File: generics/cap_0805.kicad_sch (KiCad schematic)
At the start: 2 parts

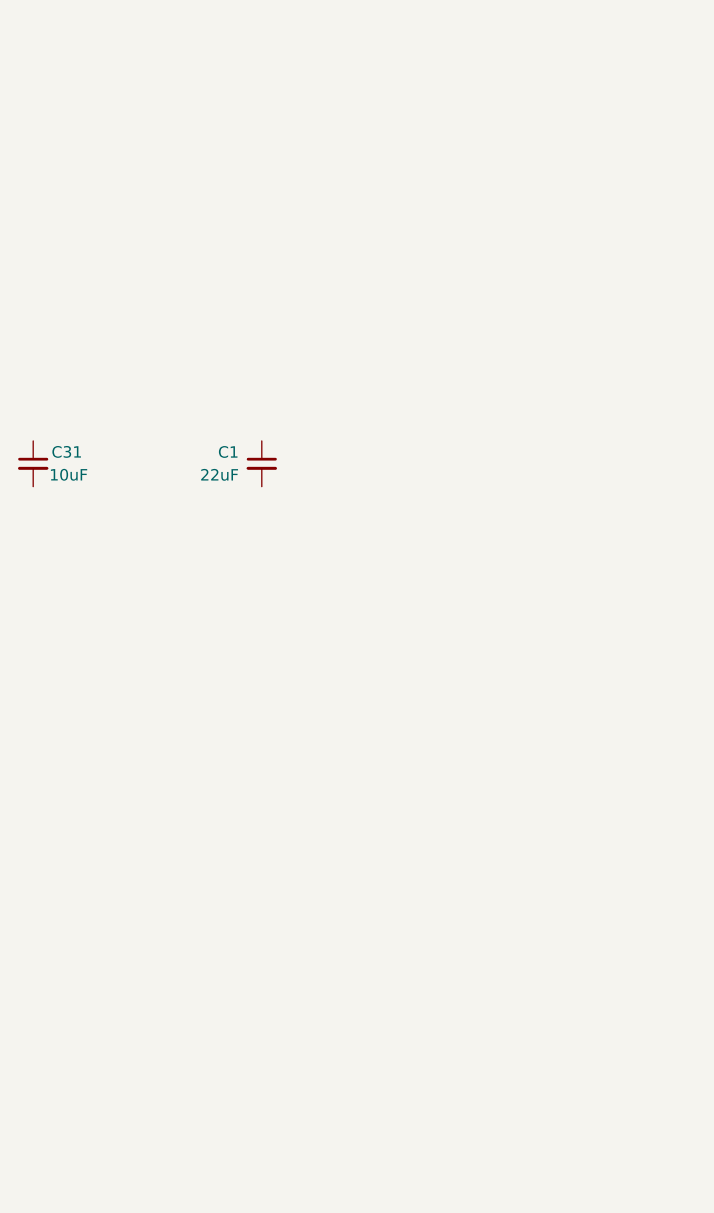
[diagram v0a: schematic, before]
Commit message: Add ESP32 and relevant peripherals
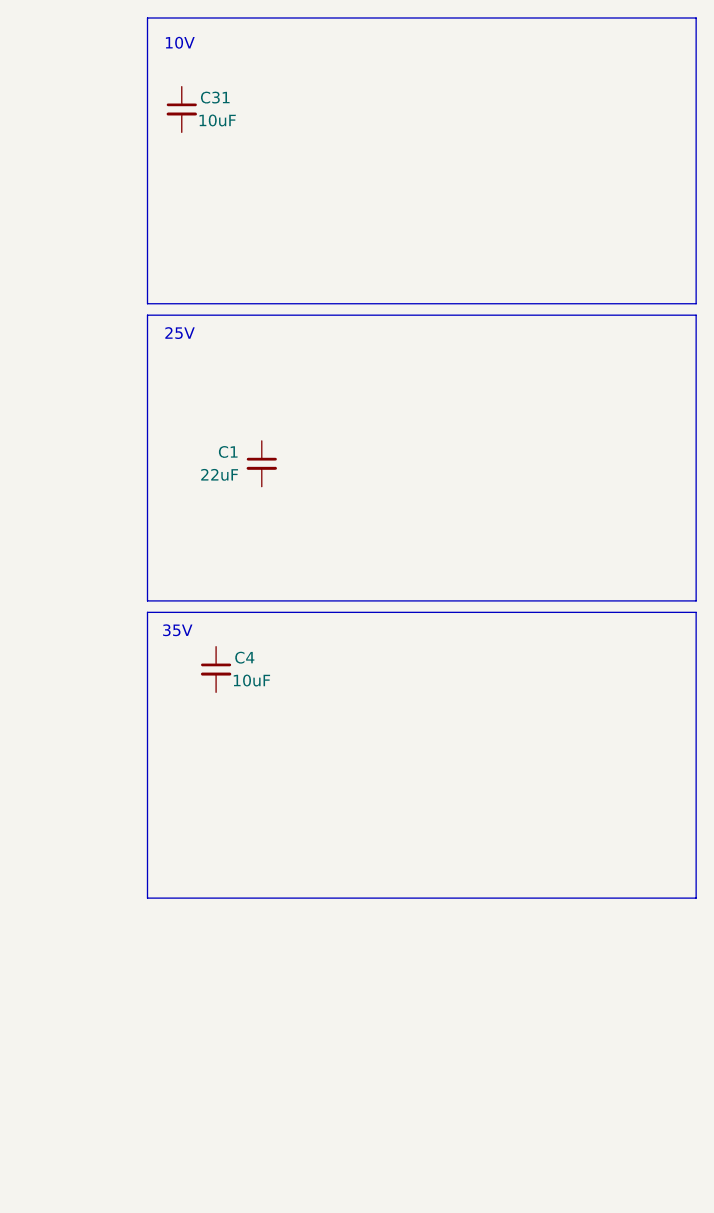
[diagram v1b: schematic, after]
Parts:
- added C4: 10uF, Capacitor_SMD:C_0805_2012Metric, symbol Device:C_Small
- C1: Tolerance (none) -> 20%; Votlage (none) -> 25V
- C31: Tolerance (none) -> 10%; Voltage (none) -> 10V
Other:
- note added: "10V"
- note added: "25V"
- note added: "35V"
- moved on the sheet: C31
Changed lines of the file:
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@@
 	(generator_version "9.0")
 	(paper "A4")
+	(rectangle
+		(start 31.75 20.32)
+		(end 92.71 52.07)
+		(stroke
+			(width 0)
+			(type default)
+		)
+		(fill
+			(type none)
+		)
+	)
+	(rectangle
+		(start 31.75 86.36)
+		(end 92.71 118.11)
+		(stroke
+			(width 0)
+			(type default)
+		)
+		(fill
+			(type none)
+		)
+	)
+	(rectangle
+		(start 31.75 53.34)
+		(end 92.71 85.09)
+		(stroke
+			(width 0)
+			(type default)
+		)
+		(fill
+			(type none)
+		)
+	)
+	(text "10V"
+		(exclude_from_sim no)
+		(at 35.306 23.368 0)
+		(effects
+			(font
+				(size 1.27 1.27)
+			)
+		)
+	)
+	(text "35V"
+		(exclude_from_sim no)
+		(at 35.052 88.646 0)
+		(effects
+			(font
+				(size 1.27 1.27)
+			)
+		)
+	)
+	(text "25V"
+		(exclude_from_sim no)
+		(at 35.306 55.626 0)
+		(effects
+			(font
+				(size 1.27 1.27)
+			)
+		)
+	)
+	(symbol
+		(lib_id "Device:C_Small")
+		(at 39.37 92.71 0)
+		(mirror y)
+		(unit 1)
+		(exclude_from_sim no)
+		(in_bom yes)
+		(on_board yes)
+		(dnp no)
+		(property "Reference" "C4"
+			(at 41.402 91.44 0)
+			(effects
+				(font
+					(size 1.27 1.27)
+				)
+				(justify right)
+			)
+		)
+		(property "Value" "10uF"
+			(at 41.148 93.98 0)
+			(effects
+				(font
+					(size 1.27 1.27)
+				)
+				(justify right)
+			)
+		)
+		(property "Footprint" "Capacitor_SMD:C_0805_2012Metric"
+			(at 39.37 92.71 0)
+			(effects
+				(font
+					(size 1.27 1.27)
+				)
+				(hide yes)
+			)
+		)
+		(property "Datasheet" "~"
+			(at 39.37 92.71 0)
+			(effects
+				(font
+					(size 1.27 1.27)
+				)
+				(hide yes)
+			)
+		)
+		(property "Description" "Unpolarized capacitor, small symbol"
+			(at 39.37 92.71 0)
+			(effects
+				(font
+					(size 1.27 1.27)
+				)
+				(hide yes)
+			)
+		)
+		(property "MPN" "GRM21BR6YA106KE43L"
+			(at 39.37 92.71 0)
+			(effects
+				(font
+					(size 1.27 1.27)
+				)
+				(hide yes)
+			)
+		)
+		(property "Mfr" "Murata Electronics"
+			(at 39.37 92.71 0)
+			(effects
+				(font
+					(size 1.27 1.27)
+				)
+				(hide yes)
+			)
+		)
+		(property "Voltage" "35V"
+			(at 39.37 92.71 0)
+			(effects
+				(font
+					(size 1.27 1.27)
+				)
+				(hide yes)
+			)
+		)
+		(property "Tolerance" "10%"
+			(at 39.37 92.71 0)
+			(effects
+				(font
+					(size 1.27 1.27)
+				)
+				(hide yes)
+			)
+		)
+		(pin "2"
+		)
+		(pin "1"
+		)
+		(instances
+			(project "generics"
+				(path "/ff075d90-2677-48ca-91fd-a3a441ca4e63/fc8a1445-9d1d-43d6-bed8-e630a9984c40"
+					(reference "C4")
+					(unit 1)
+				)
+			)
+		)
+	)
 	(symbol
 		(lib_id "Device:C_Small")
@@
 			)
 		)
+		(property "Votlage" "25V"
+			(at 44.45 69.85 0)
+			(effects
+				(font
+					(size 1.27 1.27)
+				)
+				(hide yes)
+			)
+		)
+		(property "Tolerance" "20%"
+			(at 44.45 69.85 0)
+			(effects
+				(font
+					(size 1.27 1.27)
+				)
+				(hide yes)
+			)
+		)
 		(pin "2"
 		)
@@
 		)
 		(instances
-			(project "common_comps"
+			(project "generics"
 				(path "/ff075d90-2677-48ca-91fd-a3a441ca4e63/fc8a1445-9d1d-43d6-bed8-e630a9984c40"
 					(reference "C1")
@@
 	(symbol
 		(lib_id "Device:C_Small")
-		(at 19.05 69.85 0)
+		(at 35.56 30.48 0)
 		(mirror y)
 		(unit 1)
@@
 		(dnp no)
 		(property "Reference" "C31"
-			(at 21.082 68.58 0)
+			(at 37.592 29.21 0)
 			(effects
 				(font
@@
 		)
 		(property "Value" "10uF"
-			(at 20.828 71.12 0)
+			(at 37.338 31.75 0)
 			(effects
 				(font
@@
 		)
 		(property "Footprint" "Capacitor_SMD:C_0805_2012Metric"
-			(at 19.05 69.85 0)
+			(at 35.56 30.48 0)
 			(effects
 				(font
@@
 		)
 		(property "Datasheet" "~"
-			(at 19.05 69.85 0)
+			(at 35.56 30.48 0)
 			(effects
 				(font
@@
 		)
 		(property "Description" "Unpolarized capacitor, small symbol"
-			(at 19.05 69.85 0)
+			(at 35.56 30.48 0)
 			(effects
 				(font
@@
 		)
 		(property "MPN" "GRM21BR71A106KA73L"
-			(at 19.05 69.85 0)
+			(at 35.56 30.48 0)
 			(effects
 				(font
@@
 		)
 		(property "Mfr" "Murata Electronics"
-			(at 19.05 69.85 0)
+			(at 35.56 30.48 0)
+			(effects
+				(font
+					(size 1.27 1.27)
+				)
+				(hide yes)
+			)
+		)
+		(property "Voltage" "10V"
+			(at 35.56 30.48 0)
+			(effects
+				(font
+					(size 1.27 1.27)
+				)
+				(hide yes)
+			)
+		)
+		(property "Tolerance" "10%"
+			(at 35.56 30.48 0)
 			(effects
 				(font
@@
 		)
 		(instances
-			(project "common_comps"
+			(project "generics"
 				(path "/ff075d90-2677-48ca-91fd-a3a441ca4e63/fc8a1445-9d1d-43d6-bed8-e630a9984c40"
 					(reference "C31")

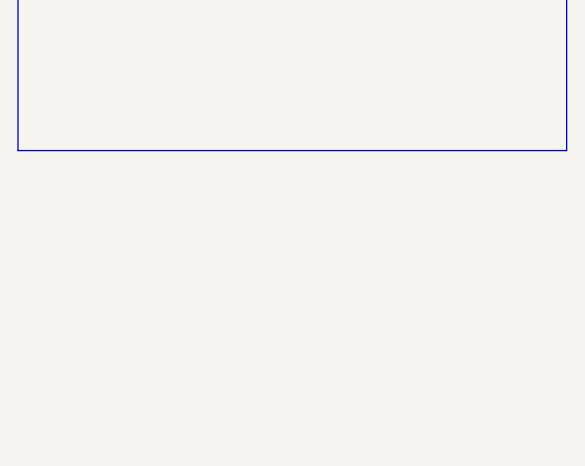
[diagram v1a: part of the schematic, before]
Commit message: Add parts for starter motor
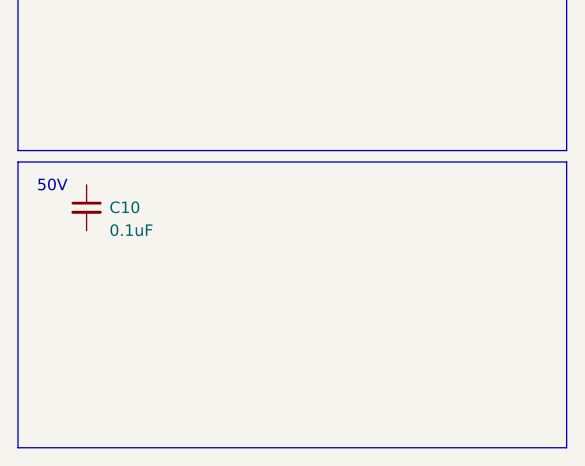
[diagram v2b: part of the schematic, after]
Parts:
- added C10: 0.1uF, Capacitor_SMD:C_0805_2012Metric, symbol Device:C_Small
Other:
- note added: "50V"
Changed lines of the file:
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@@
+		)
+	)
+	(rectangle
+		(start 31.75 119.38)
+		(end 92.71 151.13)
+		(stroke
+			(width 0)
+			(type default)
+		)
+		(fill
+			(type none)
 		)
 	)
@@
 		(exclude_from_sim no)
 		(at 35.052 88.646 0)
+		(effects
+			(font
+				(size 1.27 1.27)
+			)
+		)
+	)
+	(text "50V"
+		(exclude_from_sim no)
+		(at 35.56 122.174 0)
 		(effects
 			(font
@@
 					(unit 1)
 				)
+			)
+		)
+	)
+	(symbol
+		(lib_id "Device:C_Small")
+		(at 39.37 124.46 0)
+		(mirror y)
+		(unit 1)
+		(exclude_from_sim no)
+		(in_bom yes)
+		(on_board yes)
+		(dnp no)
+		(property "Reference" "C10"
+			(at 41.91 124.46 0)
+			(effects
+				(font
+					(size 1.27 1.27)
+				)
+				(justify right)
+			)
+		)
+		(property "Value" "0.1uF"
+			(at 41.91 127 0)
+			(effects
+				(font
+					(size 1.27 1.27)
+				)
+				(justify right)
+			)
+		)
+		(property "Footprint" "Capacitor_SMD:C_0805_2012Metric"
+			(at 39.37 124.46 0)
+			(effects
+				(font
+					(size 1.27 1.27)
+				)
+				(hide yes)
+			)
+		)
+		(property "Datasheet" "~"
+			(at 39.37 124.46 0)
+			(effects
+				(font
+					(size 1.27 1.27)
+				)
+				(hide yes)
+			)
+		)
+		(property "Description" "Unpolarized capacitor, small symbol"
+			(at 39.37 124.46 0)
+			(effects
+				(font
+					(size 1.27 1.27)
+				)
+				(hide yes)
+			)
+		)
+		(property "MPN" "CL21B104KBCNNNC"
+			(at 39.37 124.46 0)
+			(effects
+				(font
+					(size 1.27 1.27)
+				)
+				(hide yes)
+			)
+		)
+		(property "Mfr" "Samsung"
+			(at 39.37 124.46 0)
+			(effects
+				(font
+					(size 1.27 1.27)
+				)
+				(hide yes)
+			)
+		)
+		(property "JLCPCB_PN" "C1711"
+			(at 39.37 124.46 0)
+			(effects
+				(font
+					(size 1.27 1.27)
+				)
+				(hide yes)
+			)
+		)
+		(property "Package" "0805"
+			(at 39.37 124.46 0)
+			(effects
+				(font
+					(size 1.27 1.27)
+				)
+				(hide yes)
+			)
+		)
+		(property "Voltage" "50V"
+			(at 39.37 124.46 0)
+			(effects
+				(font
+					(size 1.27 1.27)
+				)
+				(hide yes)
+			)
+		)
+		(property "Tolerance" "10%"
+			(at 39.37 124.46 0)
+			(effects
+				(font
+					(size 1.27 1.27)
+				)
+				(hide yes)
+			)
+		)
+		(property "Dielectric_Class" "X7R"
+			(at 39.37 124.46 0)
+			(effects
+				(font
+					(size 1.27 1.27)
+				)
+				(hide yes)
+			)
+		)
+		(pin "2"
+		)
+		(pin "1"
+		)
+		(instances
+			(project "generics"
+				(path "/ff075d90-2677-48ca-91fd-a3a441ca4e63/fc8a1445-9d1d-43d6-bed8-e630a9984c40"
+					(reference "C10")
+					(unit 1)
+				)
